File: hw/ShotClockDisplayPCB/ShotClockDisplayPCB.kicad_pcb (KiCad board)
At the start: 4 copper layers, 54.5 x 54 mm, 5 parts, among them J1 Conn_01x05_Socket, J2 Conn_01x05_Socket, J3 Conn_01x05_Socket, J4 Conn_01x05_Socket, U1 S6B-PH-K-S-(LF)(SN)

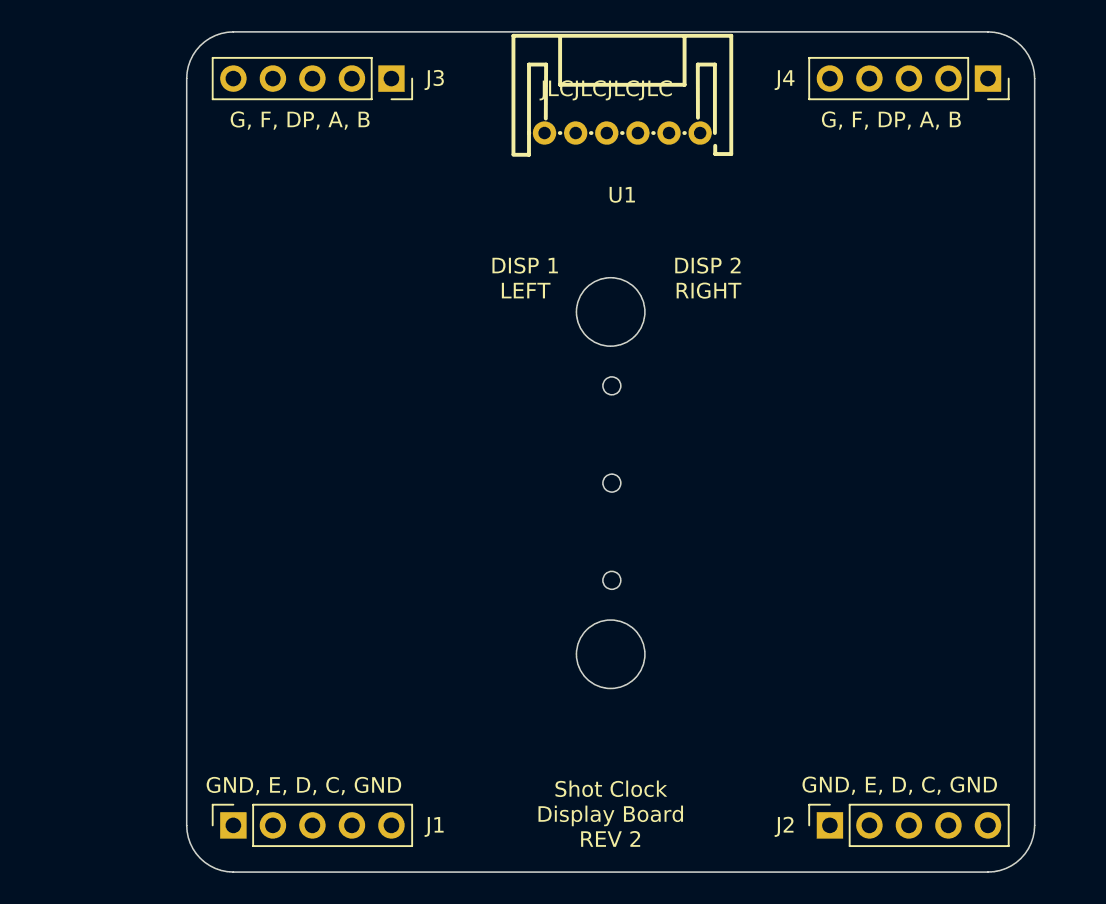
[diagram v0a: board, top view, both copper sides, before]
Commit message: Started on display board rework
added new footprints
added HW select shunts/jumpers
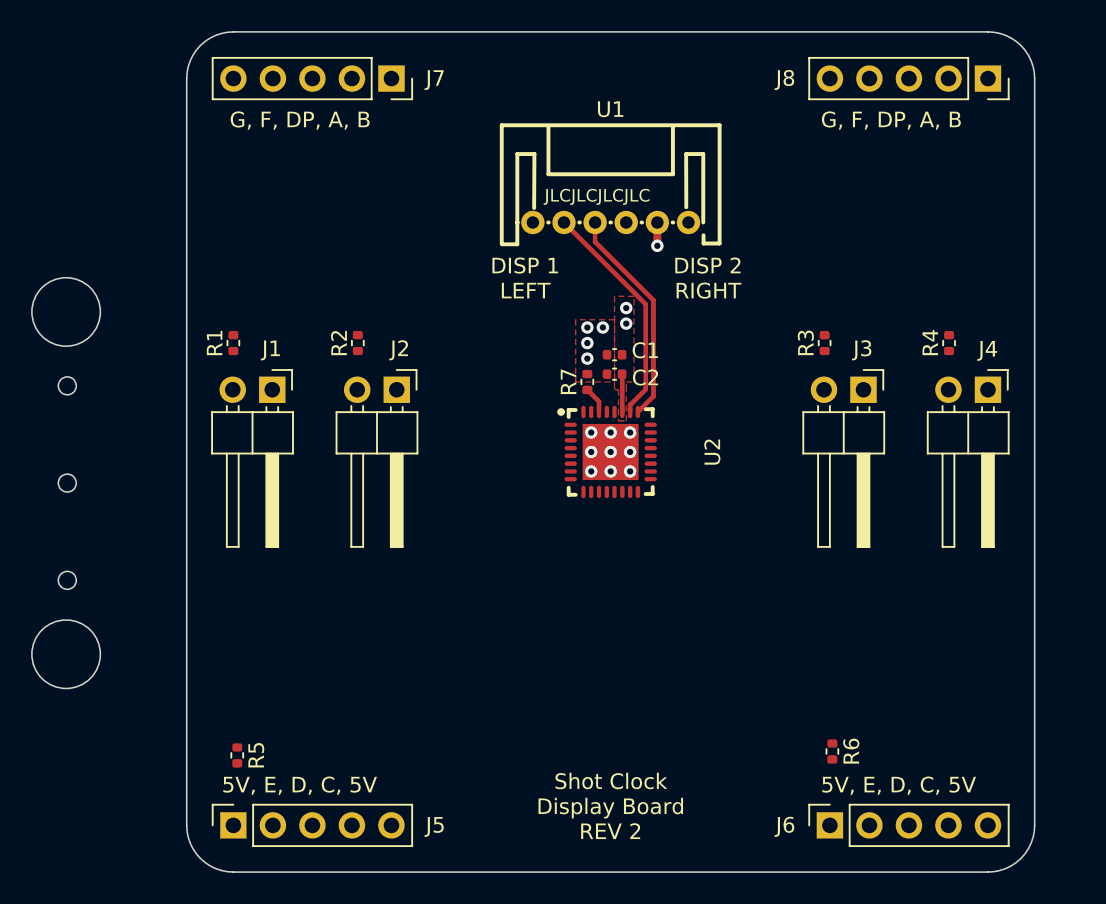
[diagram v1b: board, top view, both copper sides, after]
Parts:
- added C1: 100p, Capacitor_SMD:C_0402_1005Metric, F.Cu at (52.8, 45.8)
- added C2: 10u, Capacitor_SMD:C_0402_1005Metric, F.Cu at (52.8, 47.0)
- added J1: Conn_01x02_Pin, Connector_PinHeader_2.54mm:PinHeader_1x02_P2.54mm_Horizontal, F.Cu at (30.8, 48.0)
- added J2: Conn_01x02_Pin, Connector_PinHeader_2.54mm:PinHeader_1x02_P2.54mm_Horizontal, F.Cu at (38.8, 48.0)
- added J3: Conn_01x02_Pin, Connector_PinHeader_2.54mm:PinHeader_1x02_P2.54mm_Horizontal, F.Cu at (68.8, 48.0)
- added J4: Conn_01x02_Pin, Connector_PinHeader_2.54mm:PinHeader_1x02_P2.54mm_Horizontal, F.Cu at (76.8, 48.0)
- added R1: 10k, Resistor_SMD:R_0402_1005Metric, F.Cu at (28.2, 45.0)
- added R2: 10k, Resistor_SMD:R_0402_1005Metric, F.Cu at (36.2, 45.0)
- added R3: 10k, Resistor_SMD:R_0402_1005Metric, F.Cu at (66.2, 45.0)
- added R4: 10k, Resistor_SMD:R_0402_1005Metric, F.Cu at (74.2, 45.0)
- added R5: 100r, Resistor_SMD:R_0402_1005Metric, F.Cu at (28.5, 71.5)
- added R6: 100r, Resistor_SMD:R_0402_1005Metric, F.Cu at (66.8, 71.2)
- added R7: 1k, Resistor_SMD:R_0402_1005Metric, F.Cu at (51.0, 47.5)
- added U2: TLC59116IRHBR, TLC59116IRHBR:PG-VQFN-32_L5.0-W5.0-P0.50-BL-EP3.6, F.Cu at (52.5, 52.0)
- moved U1 5.80 mm to (52.5, 37.2)
- renumbered J1 to J5, J2 to J6, J3 to J7, J4 to J8
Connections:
- J5 pad 1: GND -> /Segment Display Connectors/5V_CONN1
- J5 pad 2: /Segment Display Connectors/SEG1_E -> SEG1_E
- J5 pad 3: /Segment Display Connectors/SEG1_D -> SEG1_D
- J5 pad 4: /Segment Display Connectors/SEG1_C -> SEG1_C
- J5 pad 5: GND -> /Segment Display Connectors/5V_CONN1
- J6 pad 1: GND -> /Segment Display Connectors/5V_CONN2
- J6 pad 2: /Segment Display Connectors/SEG2_E -> SEG2_E
- J6 pad 3: /Segment Display Connectors/SEG2_D -> SEG2_D
- J6 pad 4: /Segment Display Connectors/SEG2_C -> SEG2_C
- J6 pad 5: GND -> /Segment Display Connectors/5V_CONN2
- J7 pad 1: /Segment Display Connectors/SEG1_B -> SEG1_B
- J7 pad 2: /Segment Display Connectors/SEG1_A -> SEG1_A
- J7 pad 3: /Segment Display Connectors/SEG1_DP -> SEG1_DP
- J7 pad 4: /Segment Display Connectors/SEG1_F -> SEG1_F
- J7 pad 5: /Segment Display Connectors/SEG1_G -> SEG1_G
- J8 pad 1: /Segment Display Connectors/SEG2_B -> SEG2_B
- J8 pad 2: /Segment Display Connectors/SEG2_A -> SEG2_A
- J8 pad 3: /Segment Display Connectors/SEG2_DP -> SEG2_DP
- J8 pad 4: /Segment Display Connectors/SEG2_F -> SEG2_F
- J8 pad 5: /Segment Display Connectors/SEG2_G -> SEG2_G
- U1 pad 1: /MainBoardConnectors/TLC59116_RESETn -> /I2C PWM IO Expander/TLC59116_RESETn
- U1 pad 4: /MainBoardConnectors/I2C1_SCL -> /I2C PWM IO Expander/I2C1_SCL
- U1 pad 5: /MainBoardConnectors/I2C1_SDA -> /I2C PWM IO Expander/I2C1_SDA
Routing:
- net /I2C PWM IO Expander/I2C1_SDA: track 0.00 -> 14.8 mm
- net /I2C PWM IO Expander/I2C1_SCL: track 0.00 -> 14.1 mm
- net +3.3V: track 0.00 -> 3.94 mm, vias 0 -> 3
- net /I2C PWM IO Expander/REXT: track 0.00 -> 1.73 mm
- net GND: vias 0 -> 13
- added copper zone on F.Cu, net +3.3V
- added copper zone on In2.Cu, net +3.3V
- added copper zone on F.Cu, net GND
- added copper zone on In1.Cu, net GND
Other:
- board size 54.5 x 54 mm -> 64.5 x 54 mm
- board text added: "5V, E, D, C, 5V"
- board text removed: "GND, E, D, C, GND"

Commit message: Redid routing on disp PCB
Added TLC chip
Routed everything
Used way more filled areas
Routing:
- net SEG2_E: track 0.00 -> 43.6 mm
- net SEG2_A: track 0.00 -> 42.9 mm, vias 0 -> 2
- net SEG1_G: track 0.00 -> 41.7 mm, vias 0 -> 2
- net SEG2_B: track 0.00 -> 40.7 mm, vias 0 -> 2
- net SEG1_E: track 0.00 -> 39.8 mm
- net SEG1_DP: track 0.00 -> 39.3 mm, vias 0 -> 2
- net SEG1_F: track 0.00 -> 38.2 mm, vias 0 -> 2
- net /I2C PWM IO Expander/A0: track 0.00 -> 38.2 mm, vias 0 -> 1
- net SEG1_D: track 0.00 -> 37.7 mm
- net SEG2_DP: track 0.00 -> 37.4 mm
- net SEG2_D: track 0.00 -> 36.0 mm
- net SEG1_A: track 0.00 -> 35.0 mm
- net SEG1_C: track 0.00 -> 34.9 mm
- net /I2C PWM IO Expander/A3: track 0.00 -> 34.8 mm, vias 0 -> 1
- net SEG2_F: track 0.00 -> 30.6 mm
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- added copper zone on B.Cu, net +5V
- added copper zone on F.Cu, net +5V
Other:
- board size 64.5 x 54 mm -> 54.5 x 54 mm
